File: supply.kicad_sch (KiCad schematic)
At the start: 0 parts

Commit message: Added components to supply
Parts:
- added D1: PU2DLWH, PU2DLWH, symbol SamacSys_Parts:PU2DLWH
- added D2: PMEG3010ER, Diode_SMD:Nexperia_CFP3_SOD-123W, symbol Diode:PMEG3010ER
- added IC1: TPS70930QDRVRQ1, SON65P200X200X80-7N, symbol SamacSys_Parts:TPS70930QDRVRQ1
- added IC10: MAX25231ATCB_V+T, SON50P300X300X80-13N, symbol SamacSys_Parts:MAX25231ATCB_V+T
- added IC2: TLS850B0TEV50ATMA1, BTS6143D, symbol SamacSys_Parts:TLS850B0TEV50ATMA1
- added L1: NRS4018T100MDGJV, NRS4018T100MDGJV, symbol SamacSys_Parts:NRS4018T100MDGJV

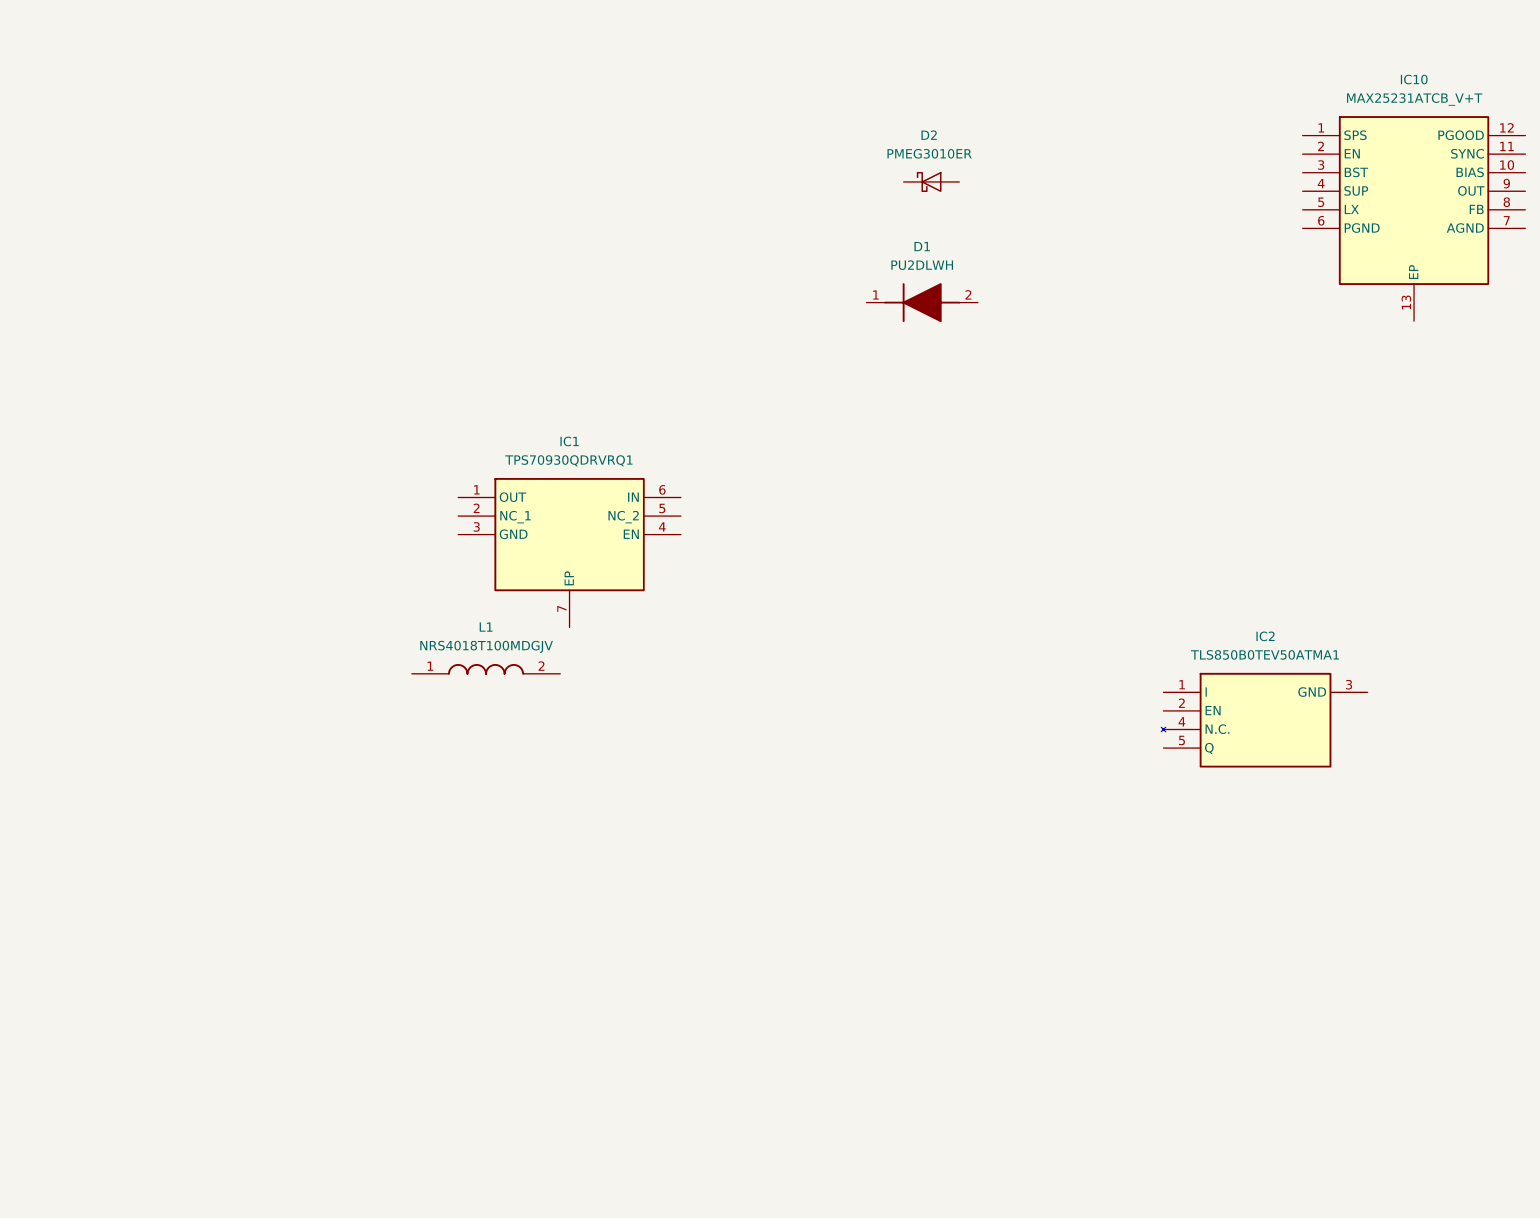
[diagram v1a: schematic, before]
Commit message: Added Wakeup, supply, more pins on MCU
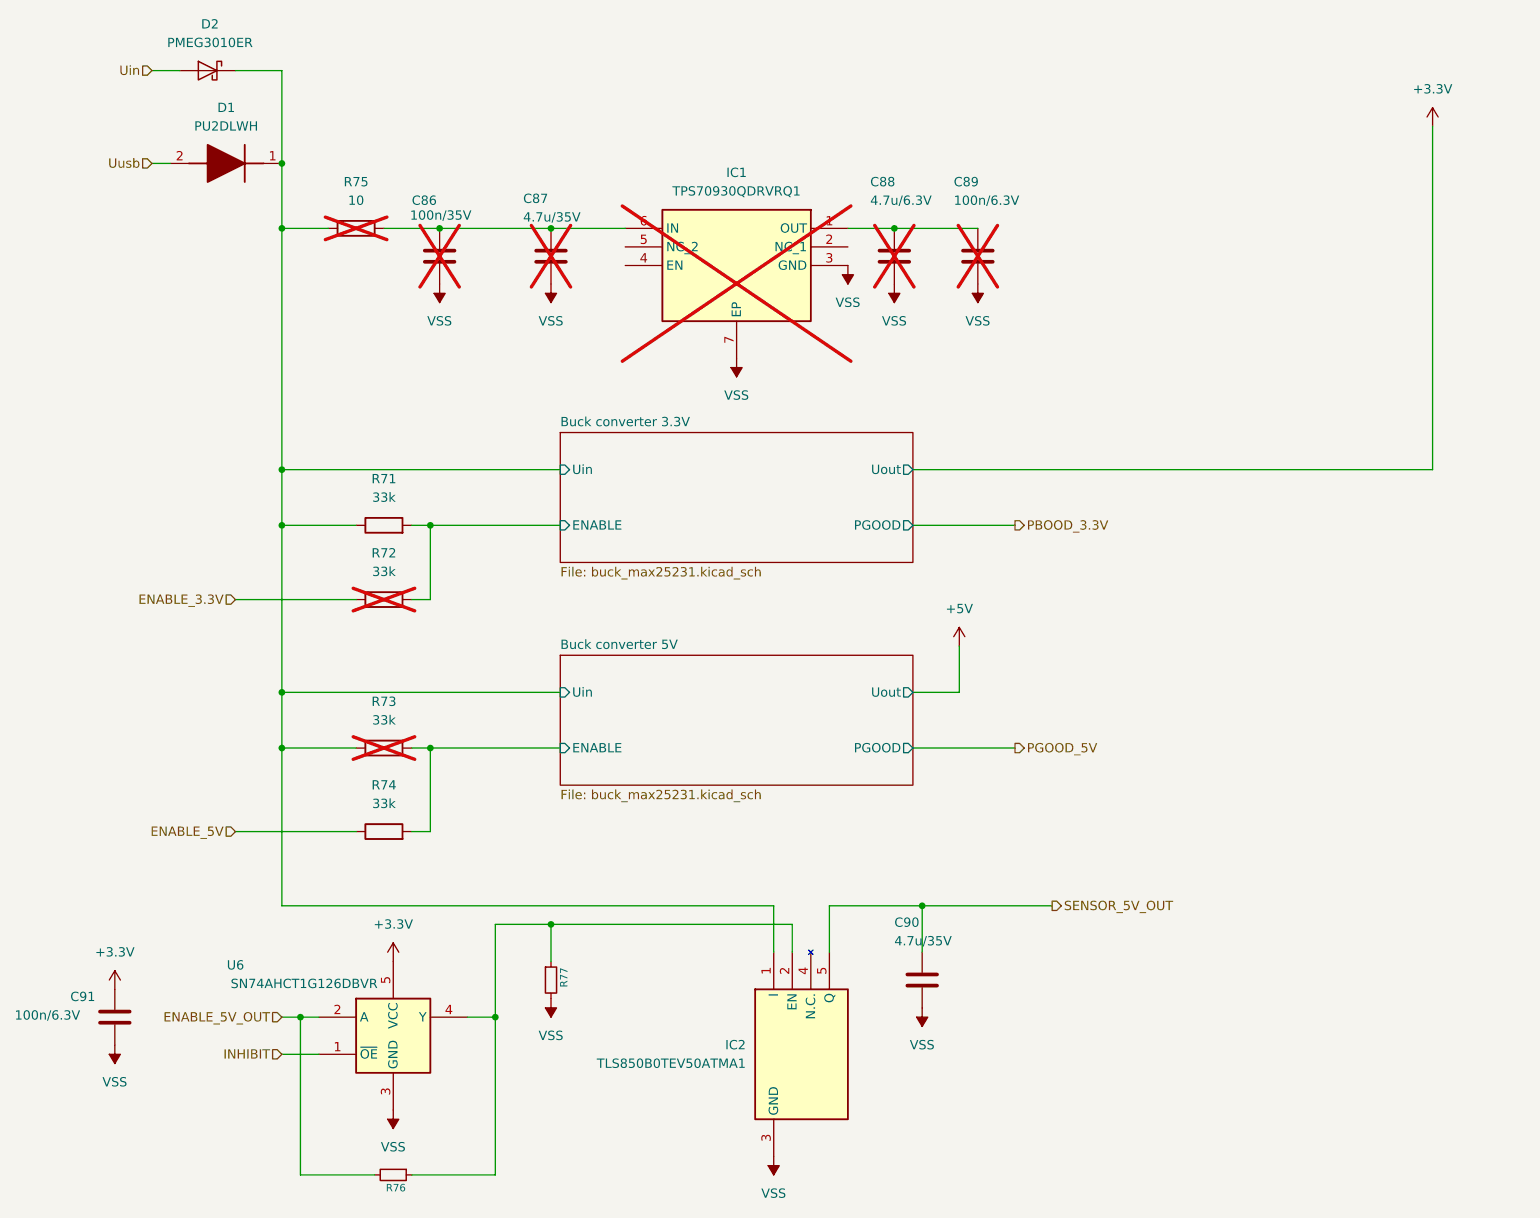
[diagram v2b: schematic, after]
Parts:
- removed IC10: MAX25231ATCB_V+T, SON50P300X300X80-13N, symbol SamacSys_Parts:MAX25231ATCB_V+T
- removed L1: NRS4018T100MDGJV, NRS4018T100MDGJV, symbol SamacSys_Parts:NRS4018T100MDGJV
- added C86: 100n/35V, Resistor_SMD:R_0805_2012Metric, symbol Device:C
- added C87, C90: 4.7u/35V, Capacitor_SMD:C_0603_1608Metric, symbol Device:C
- added C88: 4.7u/6.3V, Capacitor_SMD:C_0603_1608Metric, symbol Device:C
- added C89, C91: 100n/6.3V, Capacitor_SMD:C_0603_1608Metric, symbol Device:C
- added R71, R72, R73, R74: 33k, Resistor_SMD:R_0603_1608Metric, symbol Device:R
- added R75: 10, Resistor_SMD:R_1210_3225Metric, symbol Device:R
- added R76, R77: 10k, Resistor_SMD:R_0603_1608Metric, symbol Device:R_Small
- added U6: SN74AHCT1G126DBVR, Package_TO_SOT_SMD:SOT-23-5, symbol 74xGxx:NC7SZ125M5X
- IC1: now not fitted
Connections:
- net Buck converter 3.3V/Uin: now reaches IC2.1 (I)
- net Buck converter 3.3V/Uin: now also D1.1 (K), D2.1 (K), R71.1, R73.1, R75.1
- net at IC2.2 (EN): now also R76.1, R77.1, U6.4 (Y)
- net VSS: now reaches IC2.3 (GND)
- net VSS: now also IC1.3 (GND), IC1.7 (EP), C86.2, C87.2, C88.2, C89.2, C90.2, C91.2, R77.2, U6.3 (GND)
- net SENSOR_5V_OUT: now reaches IC2.5 (Q)
- net SENSOR_5V_OUT: now also C90.1
- net Uusb: now reaches D1.2 (A)
- net at IC1.1 (OUT): now also C88.1, C89.1
- net at IC1.6 (IN): now also C86.1, C87.1, R75.2
- net Uin: now reaches D2.2 (A)
- new net +3.3V: C91.1, U6.5 (VCC)
- new net Buck converter 3.3V/ENABLE: R71.2, R72.2
- new net Buck converter 5V/ENABLE: R73.2, R74.2
- new net ENABLE_3.3V: R72.1
- new net ENABLE_5V: R74.1
- new net ENABLE_5V_OUT: R76.2, U6.2 (A)
- new net INHIBIT: U6.1 (~{OE})
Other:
- added sheet Buck converter 3.3V (buck_max25231.kicad_sch)
- added sheet Buck converter 5V (buck_max25231.kicad_sch)
- moved on the sheet: D1, D2, IC2
